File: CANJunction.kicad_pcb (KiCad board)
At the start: 2 copper layers, 46.3 x 22.6 mm, 7 parts, among them J1 Screw_Terminal_01x02, J2 Screw_Terminal_01x06, J3 Screw_Terminal_01x02

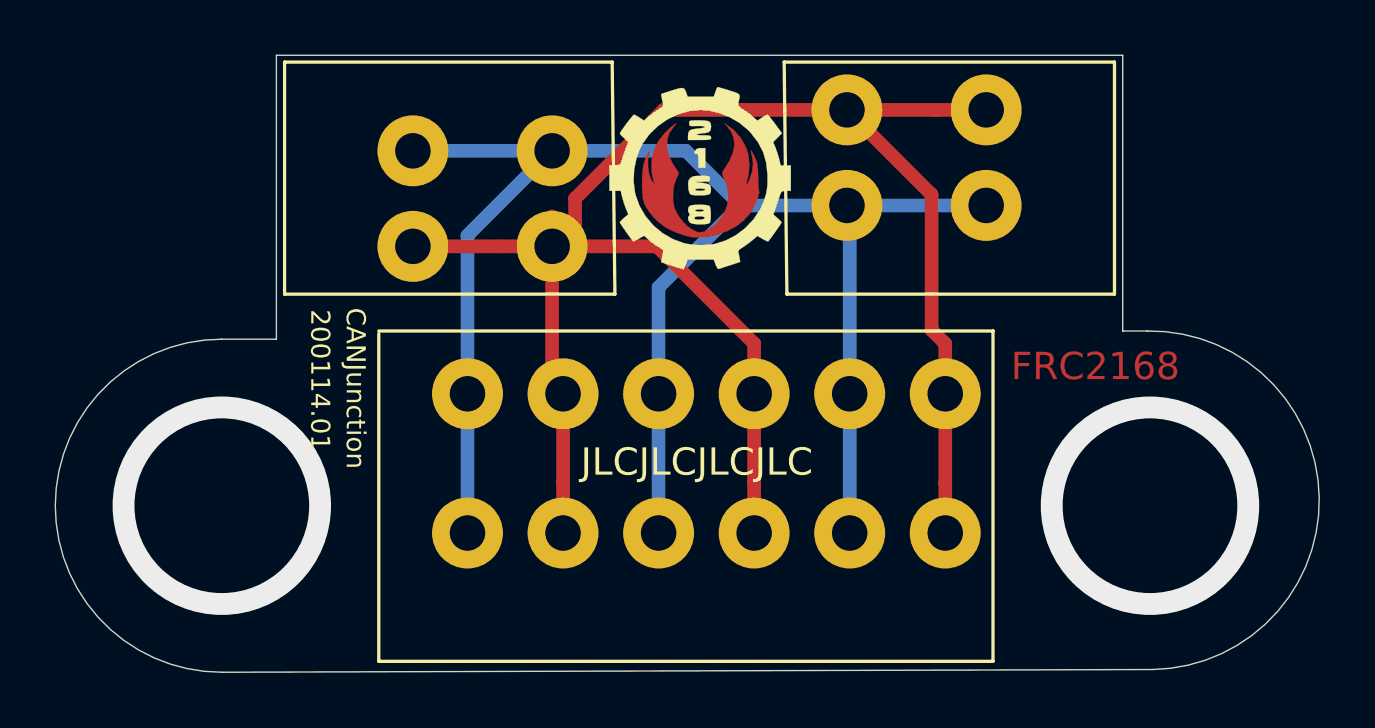
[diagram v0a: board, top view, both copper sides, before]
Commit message: add 3d models and step update gerbers w/ edge cuts in mounting 'via' re-export gerbers
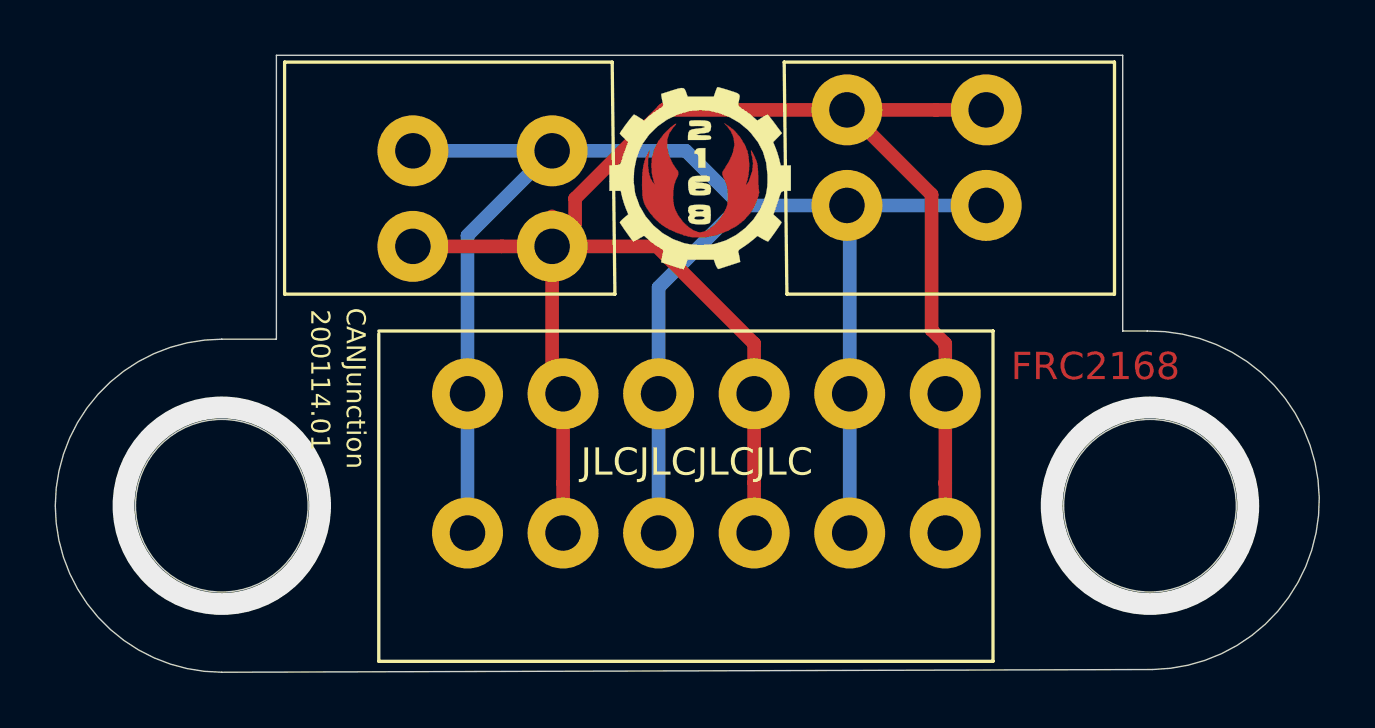
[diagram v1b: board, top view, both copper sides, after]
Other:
- outline, holes or cut-outs redrawn
